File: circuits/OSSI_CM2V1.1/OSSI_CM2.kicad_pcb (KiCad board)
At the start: 4 copper layers, 49.5 x 54.9 mm, 76 parts, among them U101 STM32L412C8T6, U103 LM75B, U104 OPA2317, X101 PINHEADER_2×5, X201 Conn_01x20_Pin, X202 Conn_01x21_Pin, Y101 10MHz

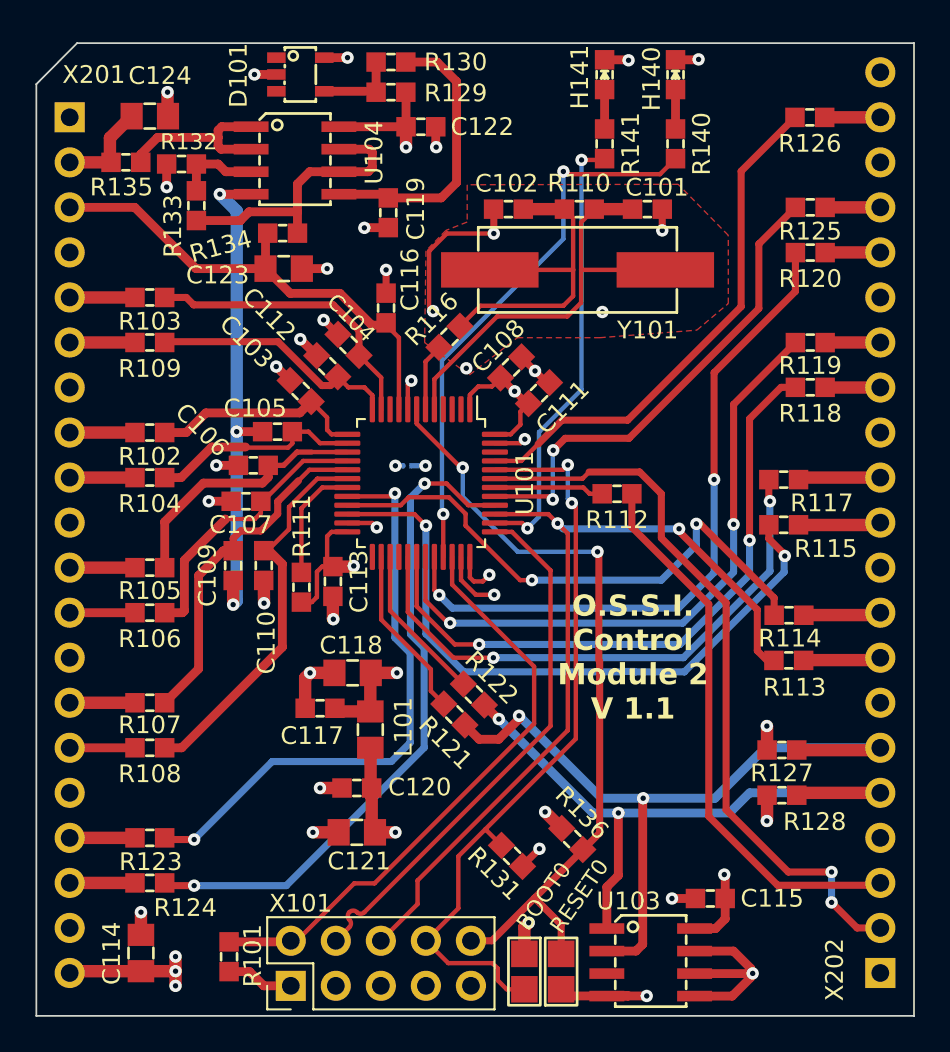
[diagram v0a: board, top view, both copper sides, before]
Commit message: minor fixes to routing to several resistor pads
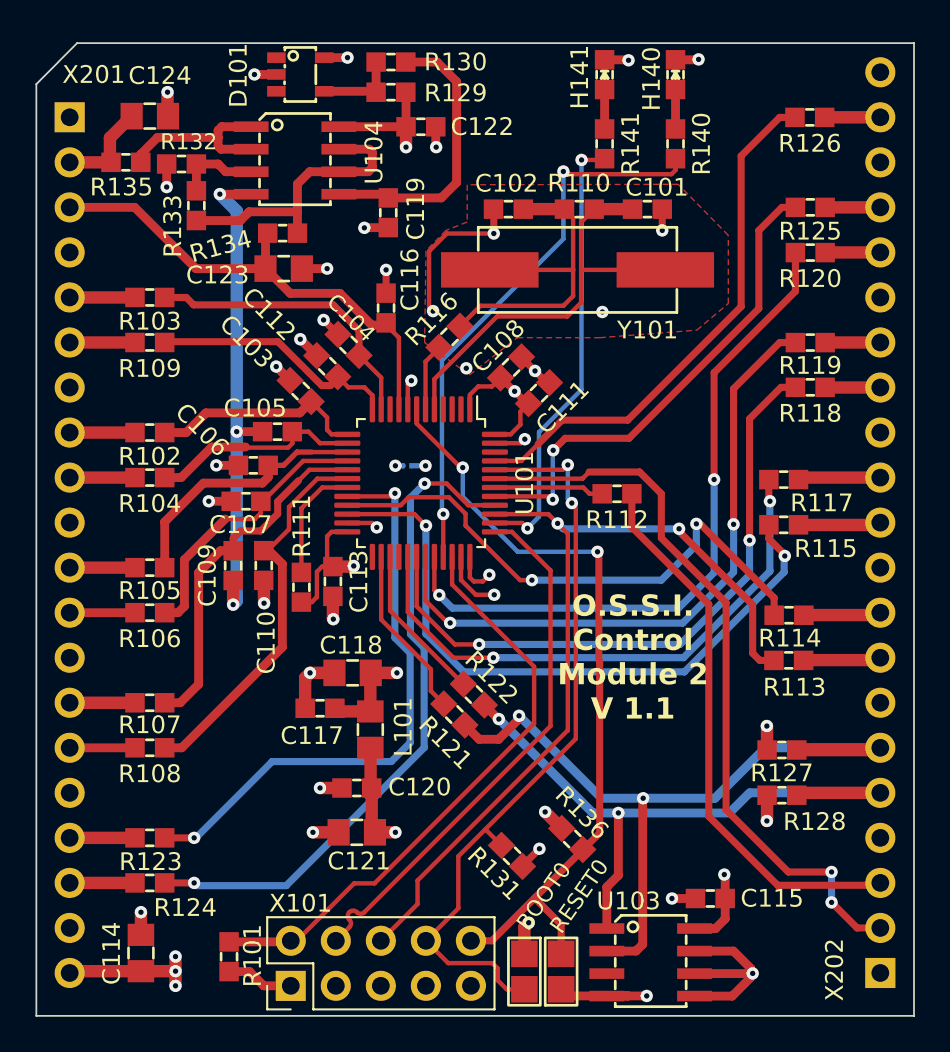
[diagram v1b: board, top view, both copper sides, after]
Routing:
- net /TRACE_SWO/PB3: track 48.4 -> 49.0 mm
- net Net-(U101C-PA7/ADC12_In12): track 19.5 -> 20.1 mm
- net Net-(U101A-PA10/T1Ch3): track 36.0 -> 36.5 mm
- net Net-(U101A-PB8): track 29.4 -> 29.9 mm
